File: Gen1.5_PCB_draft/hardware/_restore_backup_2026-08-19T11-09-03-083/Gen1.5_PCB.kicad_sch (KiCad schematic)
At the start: 45 parts, among them IC1 TJA1050T, J10 jumper2, J12 Enc2, J13 Enc3, J14 Enc4, J15 Enc5, J16 Enc6, J2 Booster, J3 Enc1, J4 jumper1, J5 Roboclaw1, J6 Roboclaw2, J7 Roboclaw3, U1 ESP32-P4-ETH, U2 4754, U8 level shifter

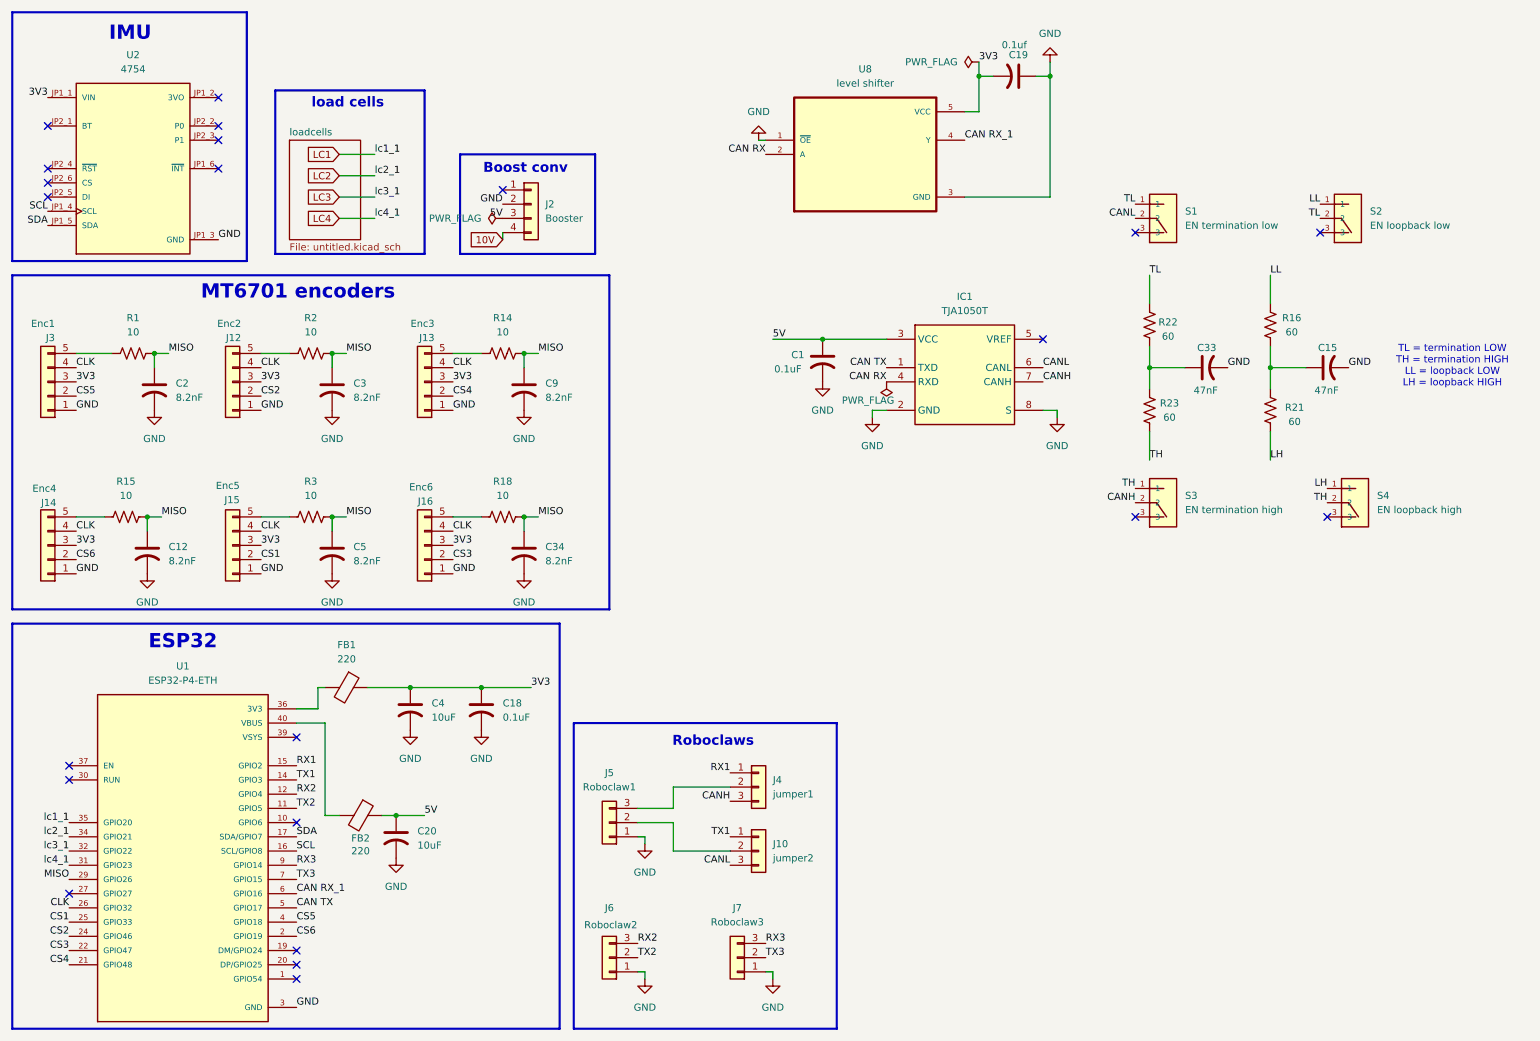
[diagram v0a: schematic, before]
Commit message: fixed sch according to last DR
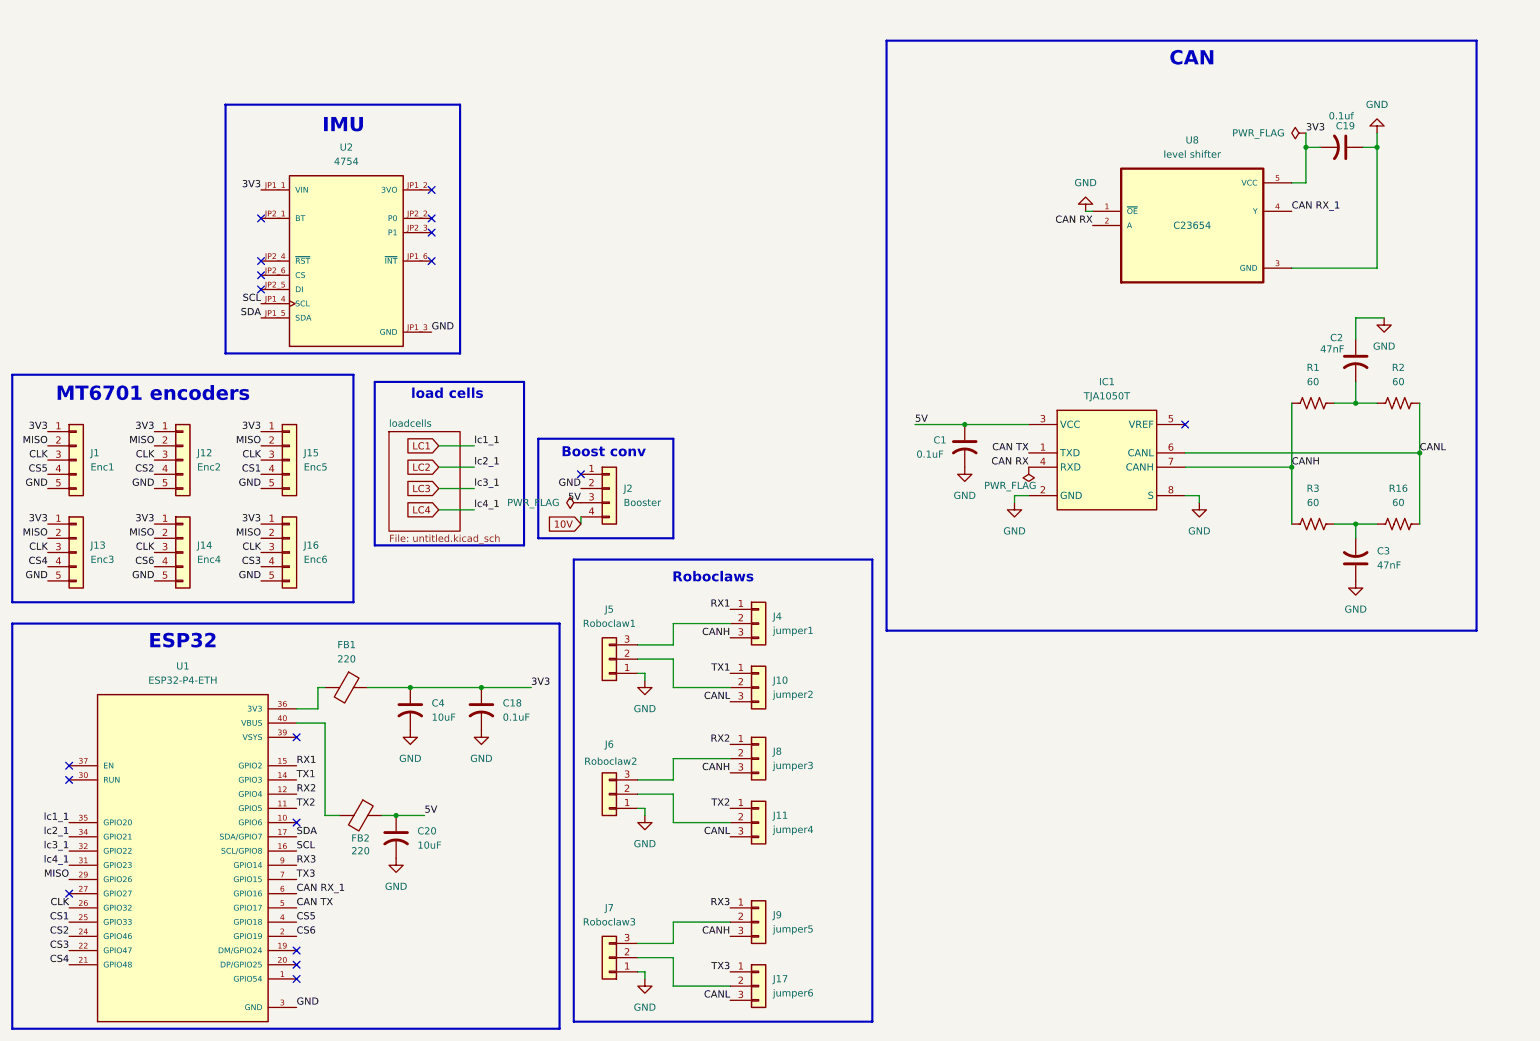
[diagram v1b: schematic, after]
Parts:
- removed C12, C34, C5, C9: 8.2nF, Gen1.5_PCB:CAP_8.2nF, symbol Device:C_US
- removed C15, C33: 47nF, Gen1.5_PCB:CAP_47nF, symbol Device:C_US
- removed J3: Enc1, Gen1.5_PCB:molex_5pin, symbol Connector_Generic:Conn_01x05
- removed R14, R15, R18: 10, Gen1.5_PCB:RES_10, symbol Device:R_US
- removed R21, R22, R23: 60, Gen1.5_PCB:RES_60, symbol Device:R_US
- removed S1: EN termination low, Gen1.5_PCB:switch, symbol Gen1.5_PCB:switch
- removed S2: EN loopback low, Gen1.5_PCB:switch, symbol Gen1.5_PCB:switch
- removed S3: EN termination high, Gen1.5_PCB:switch, symbol Gen1.5_PCB:switch
- removed S4: EN loopback high, Gen1.5_PCB:switch, symbol Gen1.5_PCB:switch
- added J1: Enc1, Gen1.5_PCB:molex_5pin, symbol Connector_Generic:Conn_01x05
- added J11: jumper4, Gen1.5_PCB:CONN_3pin_jumper, symbol Connector_Generic:Conn_01x03
- added J17: jumper6, Gen1.5_PCB:CONN_3pin_jumper, symbol Connector_Generic:Conn_01x03
- added J8: jumper3, Gen1.5_PCB:CONN_3pin_jumper, symbol Connector_Generic:Conn_01x03
- added J9: jumper5, Gen1.5_PCB:CONN_3pin_jumper, symbol Connector_Generic:Conn_01x03
- C2, C3: value 8.2nF -> 47nF; footprint Gen1.5_PCB:CAP_8.2nF -> Gen1.5_PCB:CAP_47nF; LCSC C541598 -> C3019600
- R1, R2, R3: value 10 -> 60; footprint Gen1.5_PCB:RES_10 -> Gen1.5_PCB:RES_60; LCSC C876843 -> C3994751
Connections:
- net 3V3: now also J12.1 (Pin_1), J13.1 (Pin_1), J14.1 (Pin_1), J15.1 (Pin_1), J16.1 (Pin_1), J1.1 (Pin_1); no longer J12.3 (Pin_3), J13.3 (Pin_3), J14.3 (Pin_3), J15.3 (Pin_3), J16.3 (Pin_3)
- net CANH: now also R1.1, R3.1, J8.3 (Pin_3), J9.3 (Pin_3)
- net CANL: now also R16.2, R2.2, J11.3 (Pin_3), J17.3 (Pin_3)
- net CLK: now also J12.3 (Pin_3), J13.3 (Pin_3), J14.3 (Pin_3), J15.3 (Pin_3), J16.3 (Pin_3), J1.3 (Pin_3); no longer J12.4 (Pin_4), J13.4 (Pin_4), J14.4 (Pin_4), J15.4 (Pin_4), J16.4 (Pin_4)
- net CS1: now also J15.4 (Pin_4); no longer J15.2 (Pin_2)
- net CS2: now also J12.4 (Pin_4); no longer J12.2 (Pin_2)
- net CS3: now also J16.4 (Pin_4); no longer J16.2 (Pin_2)
- net CS4: now also J13.4 (Pin_4); no longer J13.2 (Pin_2)
- net CS5: now also J1.4 (Pin_4)
- net CS6: now also J14.4 (Pin_4); no longer J14.2 (Pin_2)
- net GND: now also C2.1, C3.1, J12.5 (Pin_5), J13.5 (Pin_5), J14.5 (Pin_5), J15.5 (Pin_5), J16.5 (Pin_5), J1.5 (Pin_5); no longer C2.2, C3.2, J12.1 (Pin_1), J13.1 (Pin_1), J14.1 (Pin_1), J15.1 (Pin_1), J16.1 (Pin_1)
- net MISO: now also J12.2 (Pin_2), J13.2 (Pin_2), J14.2 (Pin_2), J15.2 (Pin_2), J16.2 (Pin_2), J1.2 (Pin_2); no longer C2.1, C3.1, R1.2, R2.2, R3.2
- net RX2: now also J8.1 (Pin_1); no longer J6.3 (Pin_3)
- net RX3: now also J9.1 (Pin_1); no longer J7.3 (Pin_3)
- net TX2: now also J11.1 (Pin_1); no longer J6.2 (Pin_2)
- net TX3: now also J17.1 (Pin_1); no longer J7.2 (Pin_2)
- net at R2.1: now also C2.2, R1.2; no longer J12.5 (Pin_5)
- net LL: no longer names the net of R16.1
- net LL: now also C3.2, R3.2
- new net: J11.2 (Pin_2), J6.2 (Pin_2)
- new net: J17.2 (Pin_2), J7.2 (Pin_2)
- new net: J7.3 (Pin_3), J9.2 (Pin_2)
- new net: J6.3 (Pin_3), J8.2 (Pin_2)
- no-connect marks 22 -> 18
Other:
- note added: "CAN"
- note removed: "TL = termination LOW TH = termination HIGH LL = loopback LOW LH = loopback HIGH"
- moved on the sheet: C1, C19, IC1, J10, J12, J13, J14, J15, J16, J2, J4, J5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
